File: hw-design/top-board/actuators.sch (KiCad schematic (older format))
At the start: 20 parts, among them P7 FOOTSWITCH, P8 FOOTSWITCH

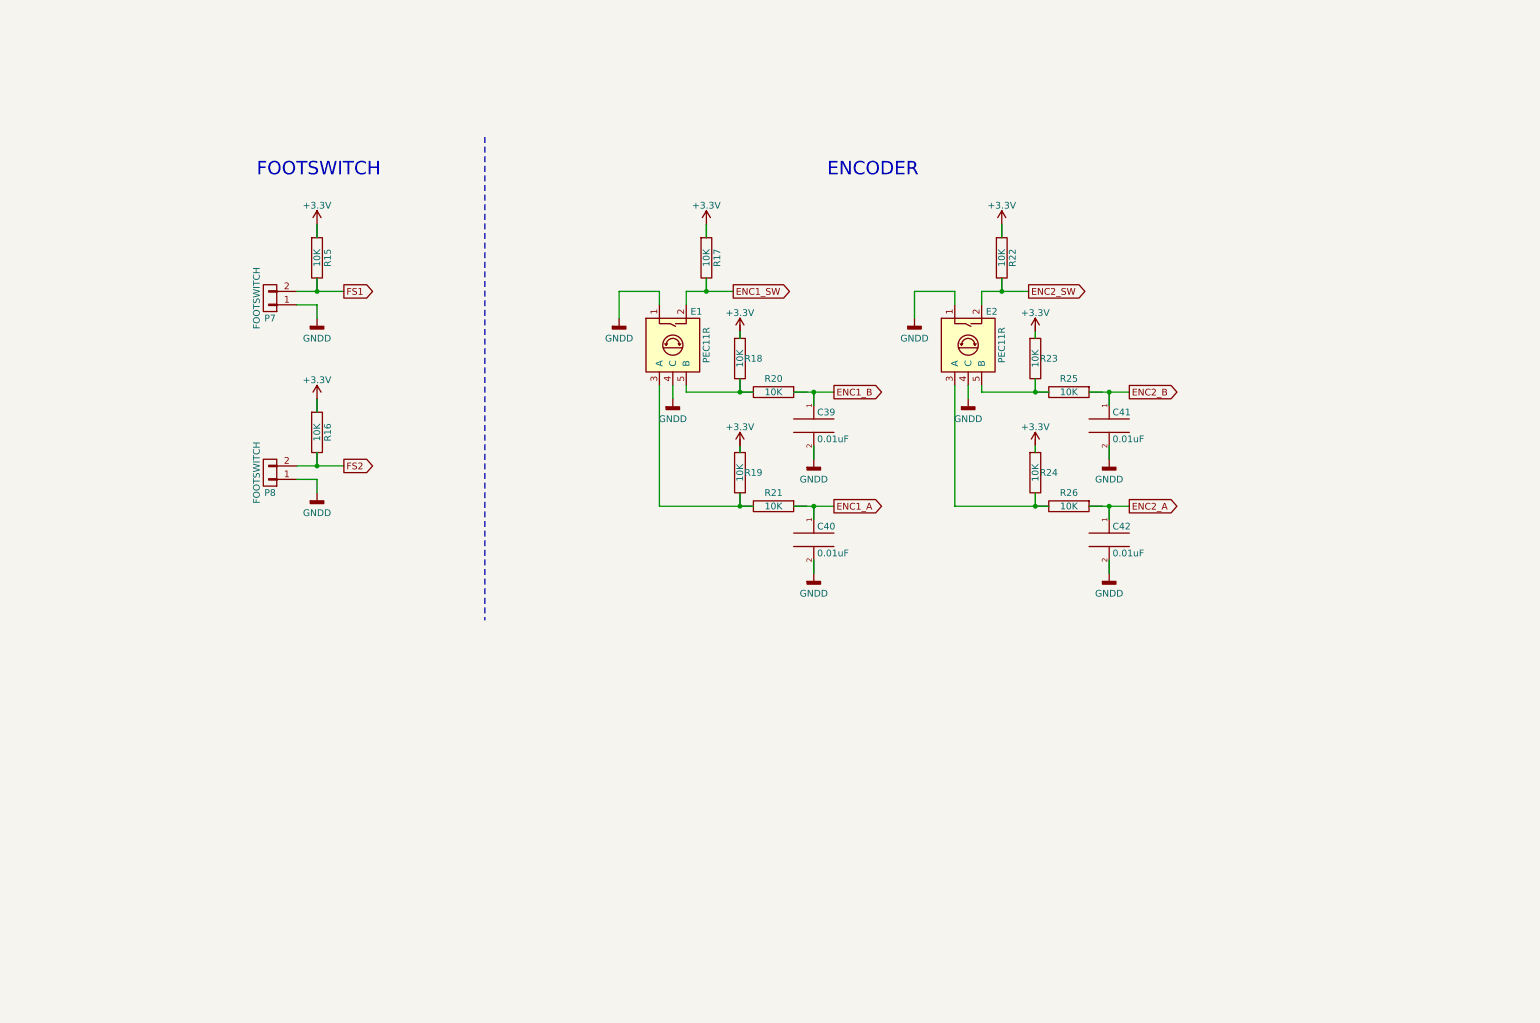
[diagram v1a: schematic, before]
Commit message: added new components and footprints
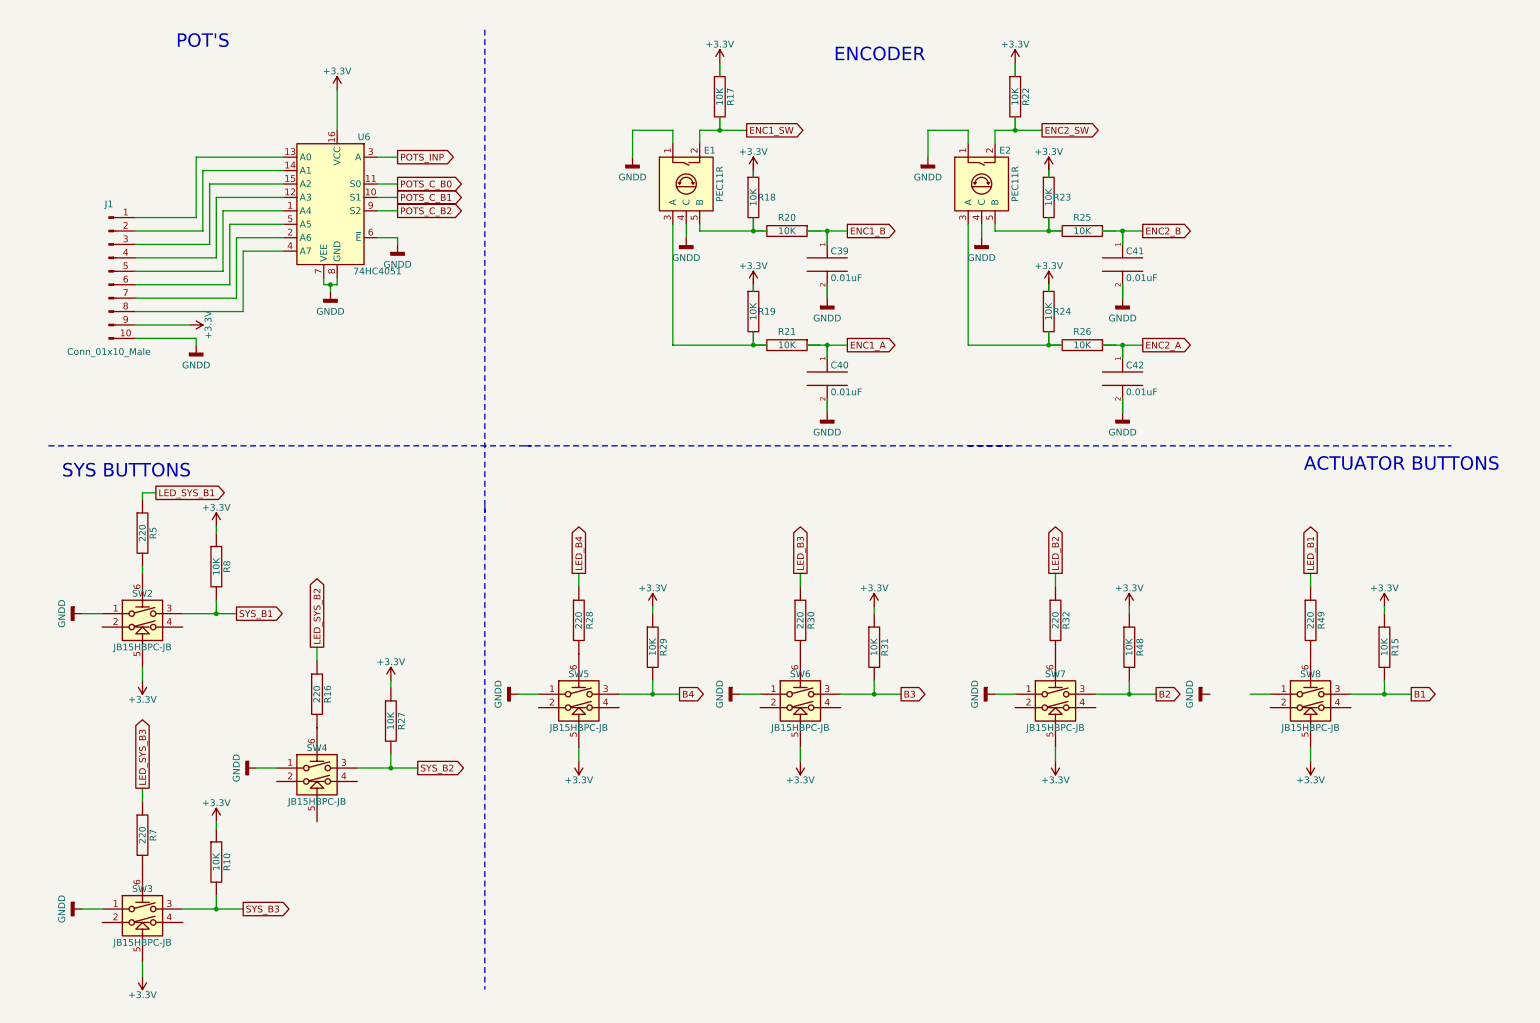
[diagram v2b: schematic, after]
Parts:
- removed P7, P8: FOOTSWITCH, Pin_Headers:Pin_Header_Angled_1x02, symbol CONN_01X02
- added J1: Conn_01x10_Male, Socket_Strips:Socket_Strip_Straight_1x10_Pitch2.54mm, symbol Conn_01x10_Male
- added R10, R27, R29, R31, R48, R8: 10K, Resistors_SMD:R_0603, symbol R
- added R28, R30, R32, R49, R5, R7: 220, Resistors_SMD:R_0603, symbol R
- added SW2, SW3, SW4, SW5, SW6, SW7, SW8: JB15HBPC-JB, buttonLED:BUTTON, symbol JB15HBPC-JB
- added U6: 74HC4051, QFN50P250X350X100-17N:QFN50P250X350X100-17N, symbol 74HC4051
- R16: value 10K -> 220
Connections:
- net labels added: B1, B2, B3, B4, LED_B1, LED_B2, LED_B3, LED_B4, LED_SYS_B1, LED_SYS_B2, LED_SYS_B3, POTS_C_B0, POTS_C_B1, POTS_C_B2, POTS_INP, SYS_B1, SYS_B2, SYS_B3
- net labels removed: FS1, FS2
- wire segments 54 -> 125
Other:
- note added: "ACTUATOR BUTTONS"
- note added: "POT'S"
- note added: "SYS BUTTONS"
- note removed: "FOOTSWITCH"
- moved on the sheet: C39, C40, C41, C42, E1, E2, R15, R17, R18, R19, R20, R21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

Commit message: sketch route of the components
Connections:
- wire segments 125 -> 137
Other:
- moved on the sheet: R26

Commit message: routing tracks
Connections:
- net labels added: POT_1, POT_2, POT_3, POT_4, POT_5, POT_6, POT_7, POT_8
- wire segments 137 -> 129
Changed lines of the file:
@@
 Text GLabel 1250 3950 2    50   Output ~ 0
 LED_SYS_B1
+$Comp
+L +3.3V #PWR098
+U 1 1 5AF2313E
+P 2450 6500
+F 0 "#PWR098" H 2450 6350 50  0001 C CNN
+F 1 "+3.3V" H 2450 6640 50  0000 C CNN
+F 2 "" H 2450 6500 60  0000 C CNN
+F 3 "" H 2450 6500 60  0000 C CNN
+	1    2450 6500
+	-1   0    0    1
+$EndComp
+Text GLabel 2100 1450 0    50   Output ~ 0
+POT_2
+Text GLabel 2100 1550 0    50   Output ~ 0
+POT_3
+Text GLabel 2100 1650 0    50   Output ~ 0
+POT_4
+Text GLabel 2100 1750 0    50   Output ~ 0
+POT_1
+Text GLabel 2100 1850 0    50   Output ~ 0
+POT_5
+Text GLabel 2100 1950 0    50   Output ~ 0
+POT_8
+Text GLabel 2100 2050 0    50   Output ~ 0
+POT_6
+Text GLabel 2100 2150 0    50   Output ~ 0
+POT_7
+Text GLabel 1200 2600 2    50   Output ~ 0
+POT_8
+Text GLabel 1200 2500 2    50   Output ~ 0
+POT_7
+Text GLabel 1200 2400 2    50   Output ~ 0
+POT_6
+Text GLabel 1200 2300 2    50   Output ~ 0
+POT_5
+Text GLabel 1200 2200 2    50   Output ~ 0
+POT_4
+Text GLabel 1200 2100 2    50   Output ~ 0
+POT_3
+Text GLabel 1200 2000 2    50   Output ~ 0
+POT_2
+Text GLabel 1200 1900 2    50   Output ~ 0
+POT_1
 Wire Wire Line
 	10150 5450 10600 5450
@@
 	1100 2700 1500 2700
 Wire Wire Line
-	1100 1900 1550 1900
-Wire Wire Line
-	1100 2000 1600 2000
-Wire Wire Line
-	1100 2100 1650 2100
-Wire Wire Line
-	1100 2200 1700 2200
-Wire Wire Line
-	1100 2300 1750 2300
-Wire Wire Line
-	1100 2400 1800 2400
-Wire Wire Line
-	1100 2500 1850 2500
-Wire Wire Line
-	1100 2600 1900 2600
-Wire Wire Line
 	2500 2400 2600 2400
 Wire Wire Line
@@
 	2600 950  2600 1250
 Wire Wire Line
-	1550 1450 2200 1450
-Wire Wire Line
-	1600 1550 2200 1550
-Wire Wire Line
-	1650 1650 2200 1650
-Wire Wire Line
-	1700 1750 2200 1750
-Wire Wire Line
-	1750 1850 2200 1850
-Wire Wire Line
-	1800 1950 2200 1950
-Wire Wire Line
-	1850 2050 2200 2050
-Wire Wire Line
-	1900 2150 2200 2150
-Wire Wire Line
 	3050 2100 3050 2050
 Wire Wire Line
@@
 	1150 3950 1150 4000
 Wire Wire Line
-	1900 2600 1900 2150
-Wire Wire Line
-	1850 2500 1850 2050
-Wire Wire Line
-	1800 2400 1800 1950
-Wire Wire Line
-	1750 2300 1750 1850
-Wire Wire Line
-	1700 2200 1700 1750
-Wire Wire Line
-	1650 2100 1650 1650
-Wire Wire Line
-	1600 2000 1600 1550
-Wire Wire Line
-	1550 1900 1550 1450
-Wire Wire Line
 	8250 3000 8300 3000
 Wire Wire Line
@@
 Wire Wire Line
 	2850 6100 2750 6100
-$Comp
-L +3.3V #PWR098
-U 1 1 5AF2313E
-P 2450 6500
-F 0 "#PWR098" H 2450 6350 50  0001 C CNN
-F 1 "+3.3V" H 2450 6640 50  0000 C CNN
-F 2 "" H 2450 6500 60  0000 C CNN
-F 3 "" H 2450 6500 60  0000 C CNN
-	1    2450 6500
-	-1   0    0    1
-$EndComp
 Wire Wire Line
 	2450 6400 2450 6500
@@
 Wire Wire Line
 	4900 5550 4700 5550
+Wire Wire Line
+	2200 1650 2100 1650
+Wire Wire Line
+	2200 1750 2100 1750
+Wire Wire Line
+	2200 1850 2100 1850
+Wire Wire Line
+	2200 1950 2100 1950
+Wire Wire Line
+	2200 2050 2100 2050
+Wire Wire Line
+	2200 2150 2100 2150
+Wire Wire Line
+	1200 1900 1100 1900
+Wire Wire Line
+	1200 2100 1100 2100
+Wire Wire Line
+	1200 2200 1100 2200
+Wire Wire Line
+	1200 2300 1100 2300
+Wire Wire Line
+	1200 2400 1100 2400
+Wire Wire Line
+	1200 2500 1100 2500
+Wire Wire Line
+	1200 2600 1100 2600
+Wire Wire Line
+	2100 1550 2200 1550
+Wire Wire Line
+	2100 1450 2200 1450
+Wire Wire Line
+	1100 2000 1200 2000
 $EndSCHEMATC

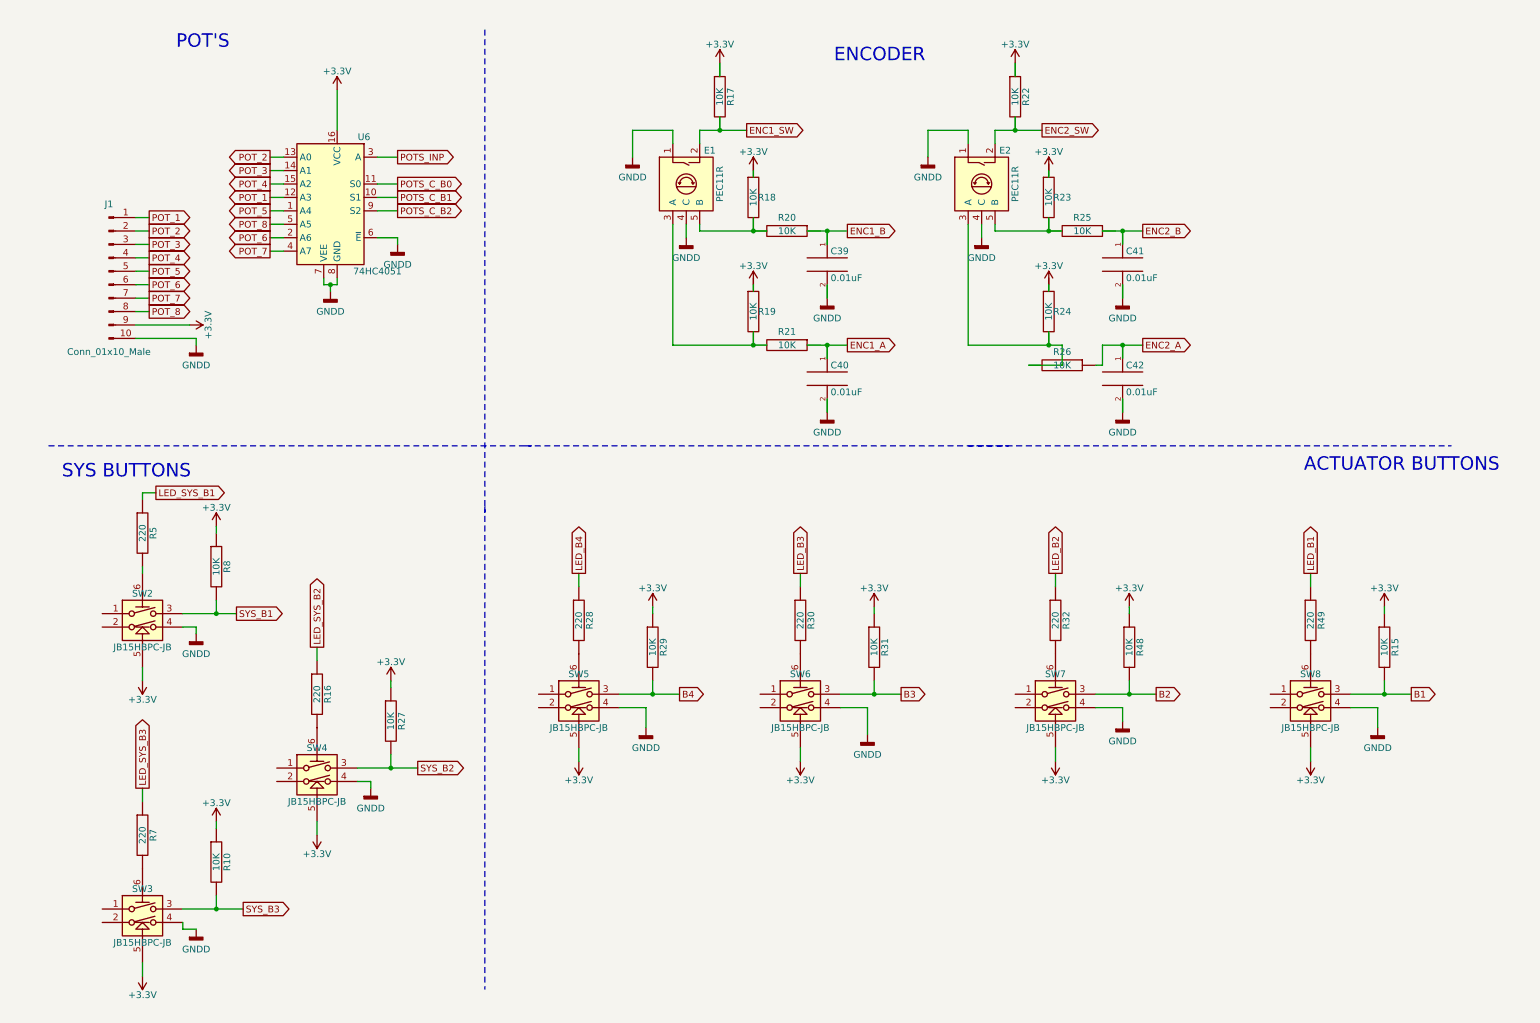
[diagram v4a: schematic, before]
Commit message: Fixed ERC & DRC tests
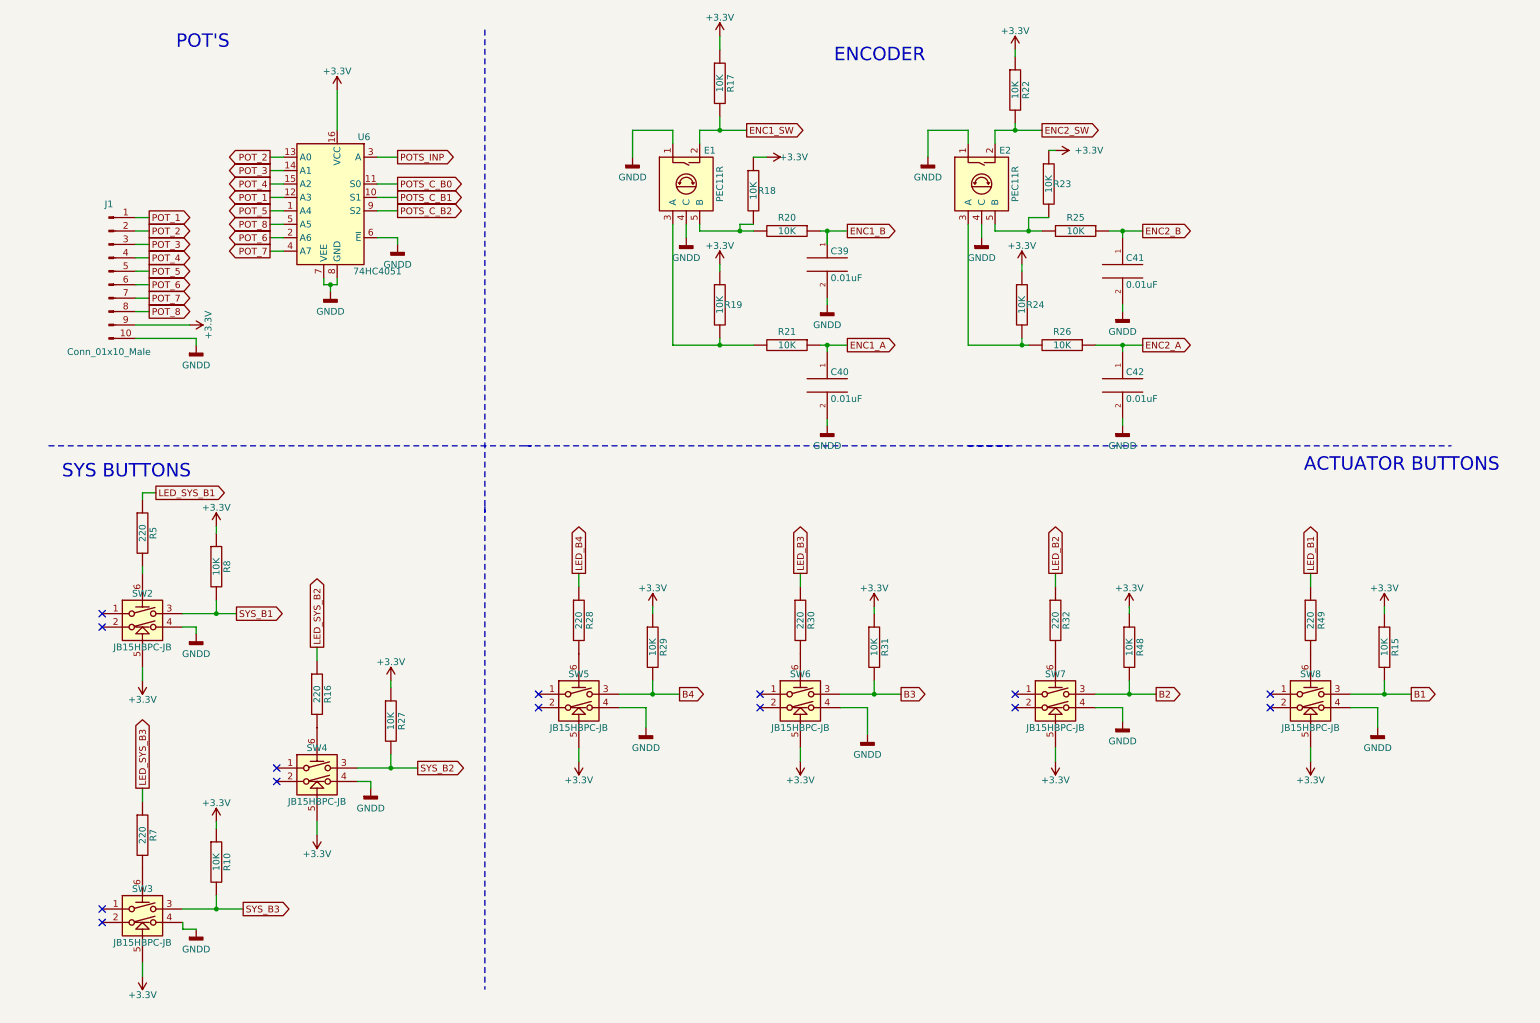
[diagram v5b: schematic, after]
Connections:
- wire segments 129 -> 127
- no-connect marks 0 -> 14
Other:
- moved on the sheet: C40, C41, C42, R17, R18, R19, R22, R23, R24, R25, R26

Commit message: Fixed button symbol
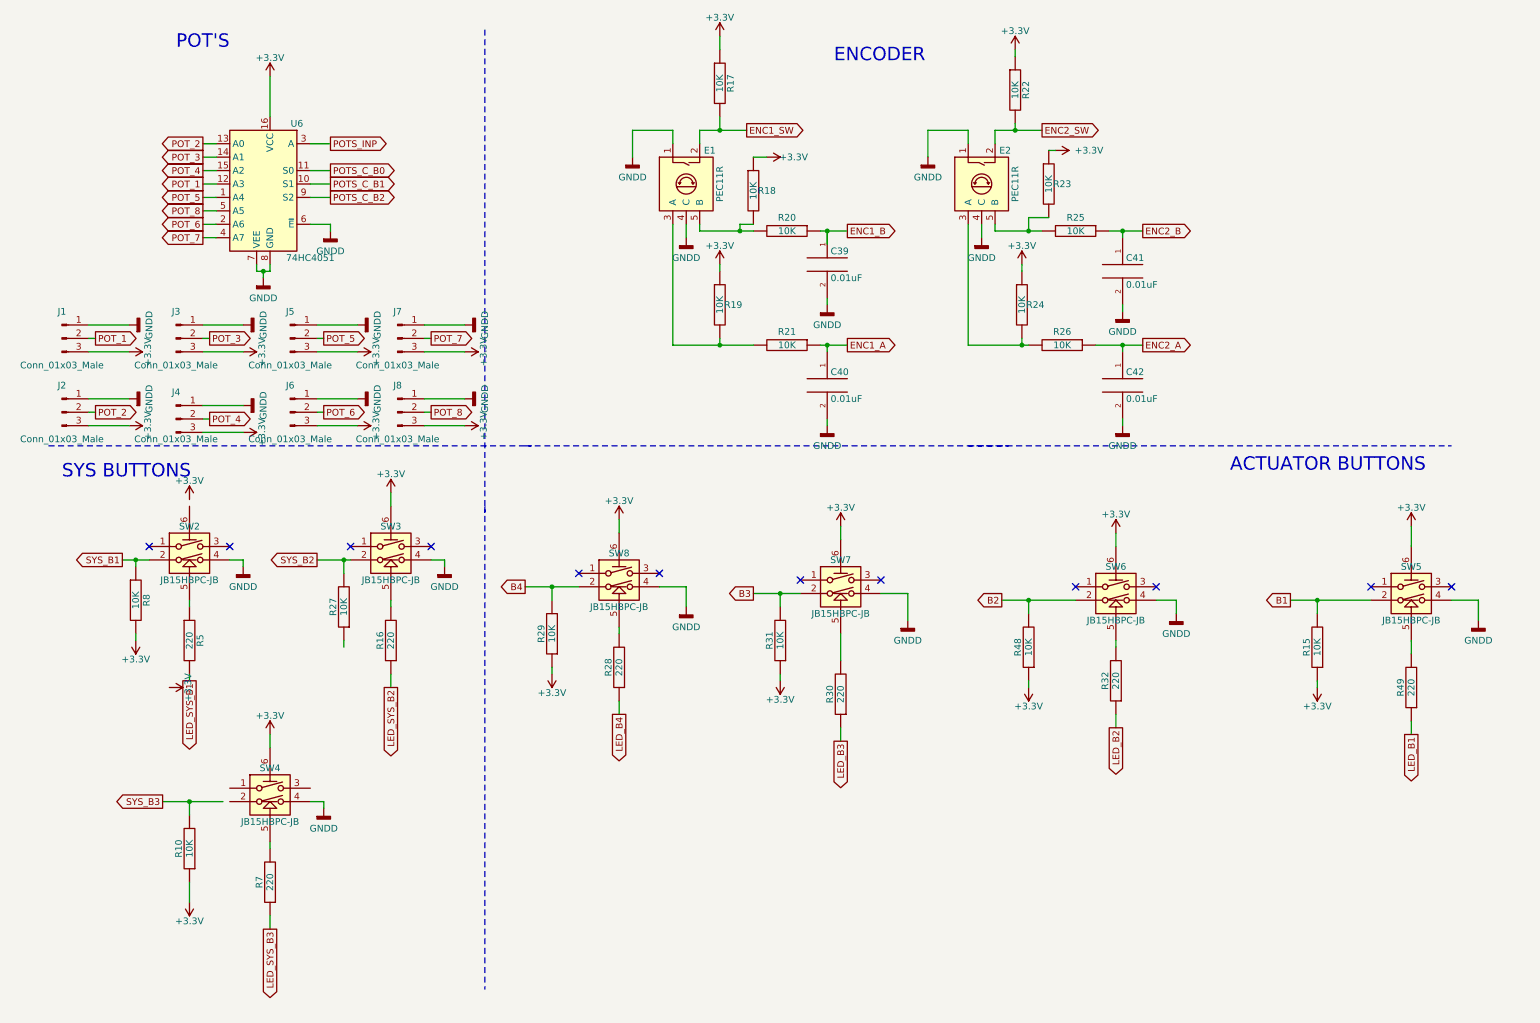
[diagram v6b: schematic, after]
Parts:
- removed J1: Conn_01x10_Male, Socket_Strips:Socket_Strip_Straight_1x10_Pitch2.54mm, symbol Conn_01x10_Male
- added J1, J2, J3, J4, J5, J6, J7, J8: Conn_01x03_Male, Pin_Headers:Pin_Header_Straight_1x03_Pitch2.54mm, symbol Conn_01x03_Male
- renumbered SW4 to SW3, SW3 to SW4, SW8 to SW5, SW7 to SW6, SW6 to SW7, SW5 to SW8
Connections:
- net +3V3: now also R8.2, SW3.6 (GND), SW4.6 (GND), SW5.6 (GND), SW6.6 (GND), SW7.6 (GND), SW8.6 (GND), J1.3 (Pin_3), J2.3 (Pin_3), J3.3 (Pin_3), J4.3 (Pin_3), J5.3 (Pin_3), J6.3 (Pin_3), J7.3 (Pin_3), J8.3 (Pin_3); no longer R27.1, R8.1, SW2.5 (LED), SW3.5 (LED), SW4.5 (LED), SW5.5 (LED), SW6.5 (LED), SW7.5 (LED), SW8.5 (LED)
- net B1: now also SW5.2; no longer SW5.3
- net B2: now also SW6.2; no longer SW6.3
- net B3: now also SW7.2; no longer SW7.3
- net B4: now also SW8.2; no longer SW8.3
- net GNDD: now also J1.1 (Pin_1), J2.1 (Pin_1), J3.1 (Pin_1), J4.1 (Pin_1), J5.1 (Pin_1), J6.1 (Pin_1), J7.1 (Pin_1), J8.1 (Pin_1)
- net LED_SYS_B1: now also R5.2; no longer R5.1
- net POT_1: now also J1.2 (Pin_2)
- net POT_2: now also J2.2 (Pin_2)
- net POT_3: now also J3.2 (Pin_2)
- net POT_4: now also J4.2 (Pin_2)
- net POT_5: now also J5.2 (Pin_2)
- net POT_6: now also J6.2 (Pin_2)
- net POT_7: now also J7.2 (Pin_2)
- net POT_8: now also J8.2 (Pin_2)
- net SYS_B1: now also R8.1, SW2.2; no longer R8.2, SW2.3
- net SYS_B2: now also SW3.2; no longer SW3.3
- net SYS_B3: no longer SW4.3
- net at R49.2: now also SW5.5 (LED); no longer SW5.6 (GND)
- net at R32.2: now also SW6.5 (LED); no longer SW6.6 (GND)
- net at R30.2: now also SW7.5 (LED); no longer SW7.6 (GND)
- net at R28.2: now also SW8.5 (LED); no longer SW8.6 (GND)
- net at R16.2: now also SW3.5 (LED); no longer SW3.6 (GND)
- net at R7.2: now also SW4.5 (LED); no longer SW4.6 (GND)
- net at SW2.6 (GND): no longer R5.2
- new net: R5.1, SW2.5 (LED)
- no-connect marks 14 -> 12
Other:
- moved on the sheet: R10, R15, R16, R27, R28, R29, R30, R31, R32, R48, R49, R5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
